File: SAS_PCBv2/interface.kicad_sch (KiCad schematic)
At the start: 26 parts, among them J10 Conn_01x04, J11 Conn_01x04, J13 Adatateur FTDI (Radio RFD900x), J14 Fan PWM, J15 Adatateur FTDI (Radio RFD900x), J4 Conn_01x02, J5 Conn_01x02, J6 Conn_01x02, J7 Conn_01x02, J8 Conn_01x02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

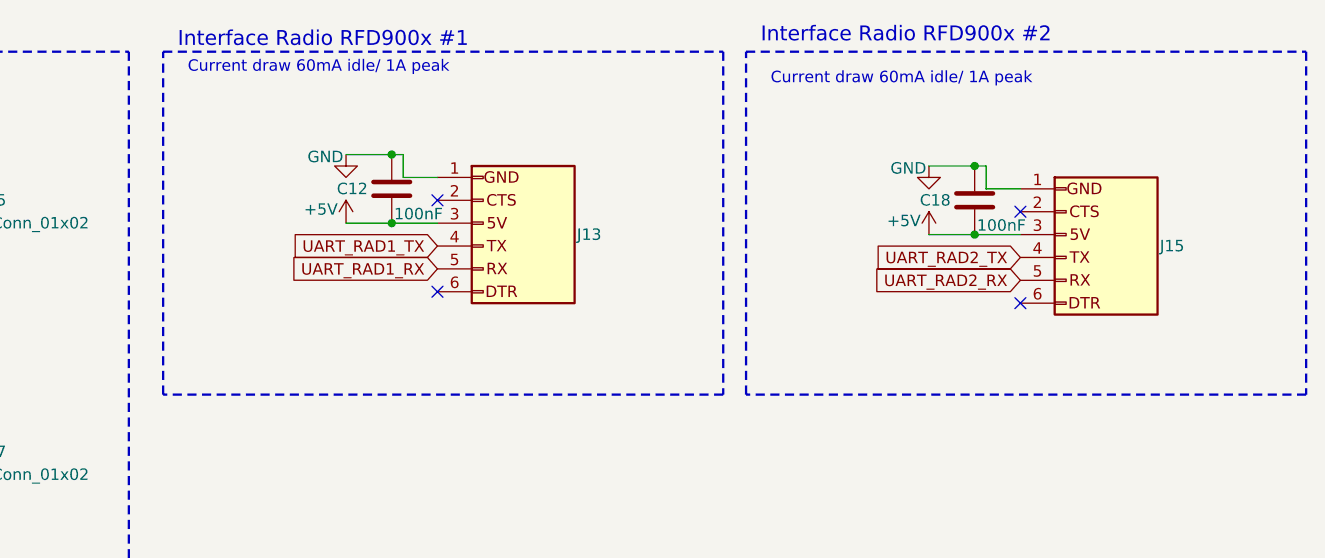
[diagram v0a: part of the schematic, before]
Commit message: Ajout du connecteur spécial pour les radios, insertion des footprints dans le PCB, fin du schéma
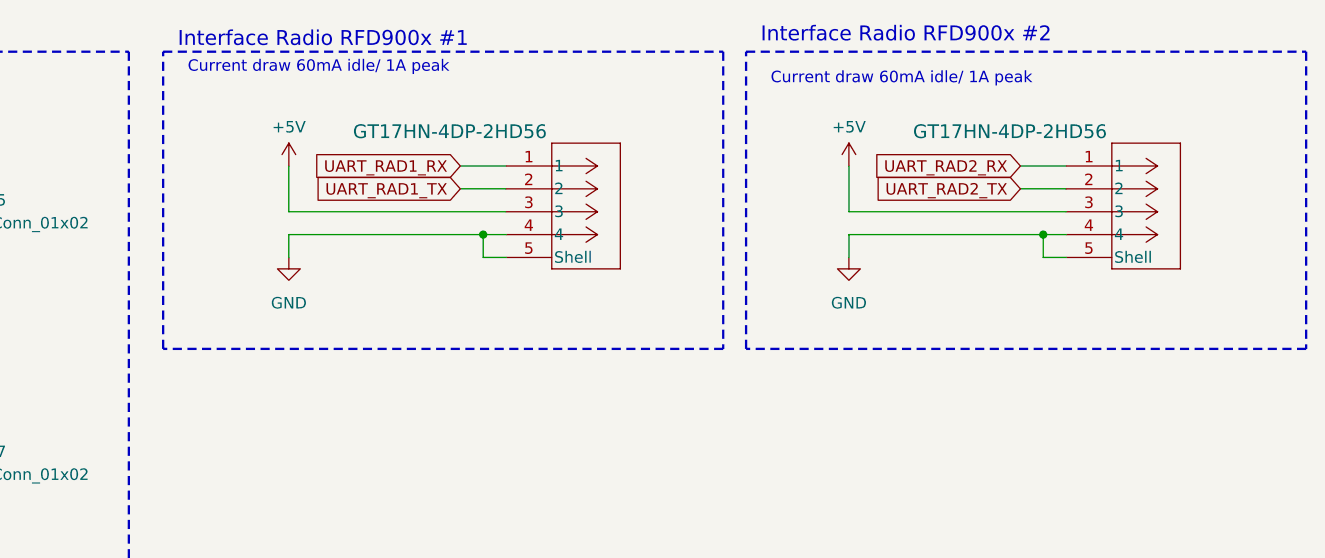
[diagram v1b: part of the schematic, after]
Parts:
- removed C12, C18: 100nF, Capacitor_THT:C_Disc_D5.0mm_W2.5mm_P2.50mm, symbol Device:C
- removed J13, J15: Adatateur FTDI (Radio RFD900x), Connector_PinHeader_2.54mm:PinHeader_1x06_P2.54mm_Vertical, symbol Connector_Generic:Conn_01x06
- added J16, J17: GT17HN-4DP-2HD56, SAS_PCBv2_footprint:CONN4_GT17HN_HIR, symbol ODB2:GT17HN-4DP-2HA56
- C3, C4, C5, C6, C7, C8: footprint Capacitor_THT:C_Disc_D5.0mm_W2.5mm_P2.50mm -> SAS_PCBv2_footprint:CAP_FG14_TDK
- J14: footprint (none) -> Connector_PinHeader_2.54mm:PinHeader_1x04_P2.54mm_Vertical
- R2, R3, R4, R5, R6, R7: Digikey (none) -> MFR-25FRF52-10K
- R8: footprint (none) -> Resistor_THT:R_Axial_DIN0207_L6.3mm_D2.5mm_P10.16mm_Horizontal; Digikey (none) -> MFR-25FRF52-10K
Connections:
- net +5V: now also J16.3, J17.3
- net GND: now also J16.4, J16.5 (Shell), J16.6 (Shell), J16.7 (Shell), J16.8 (Shell), J17.4, J17.5 (Shell), J17.6 (Shell), J17.7 (Shell), J17.8 (Shell)
- net UART_RAD1_RX: now also J16.1
- net UART_RAD1_TX: now also J16.2
- net UART_RAD2_RX: now also J17.1
- net UART_RAD2_TX: now also J17.2
- no-connect marks 4 -> 0
